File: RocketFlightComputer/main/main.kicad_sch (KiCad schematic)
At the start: 66 parts, among them Y1 32.768kHz, Y5 XRCGB24M000F2P29R0

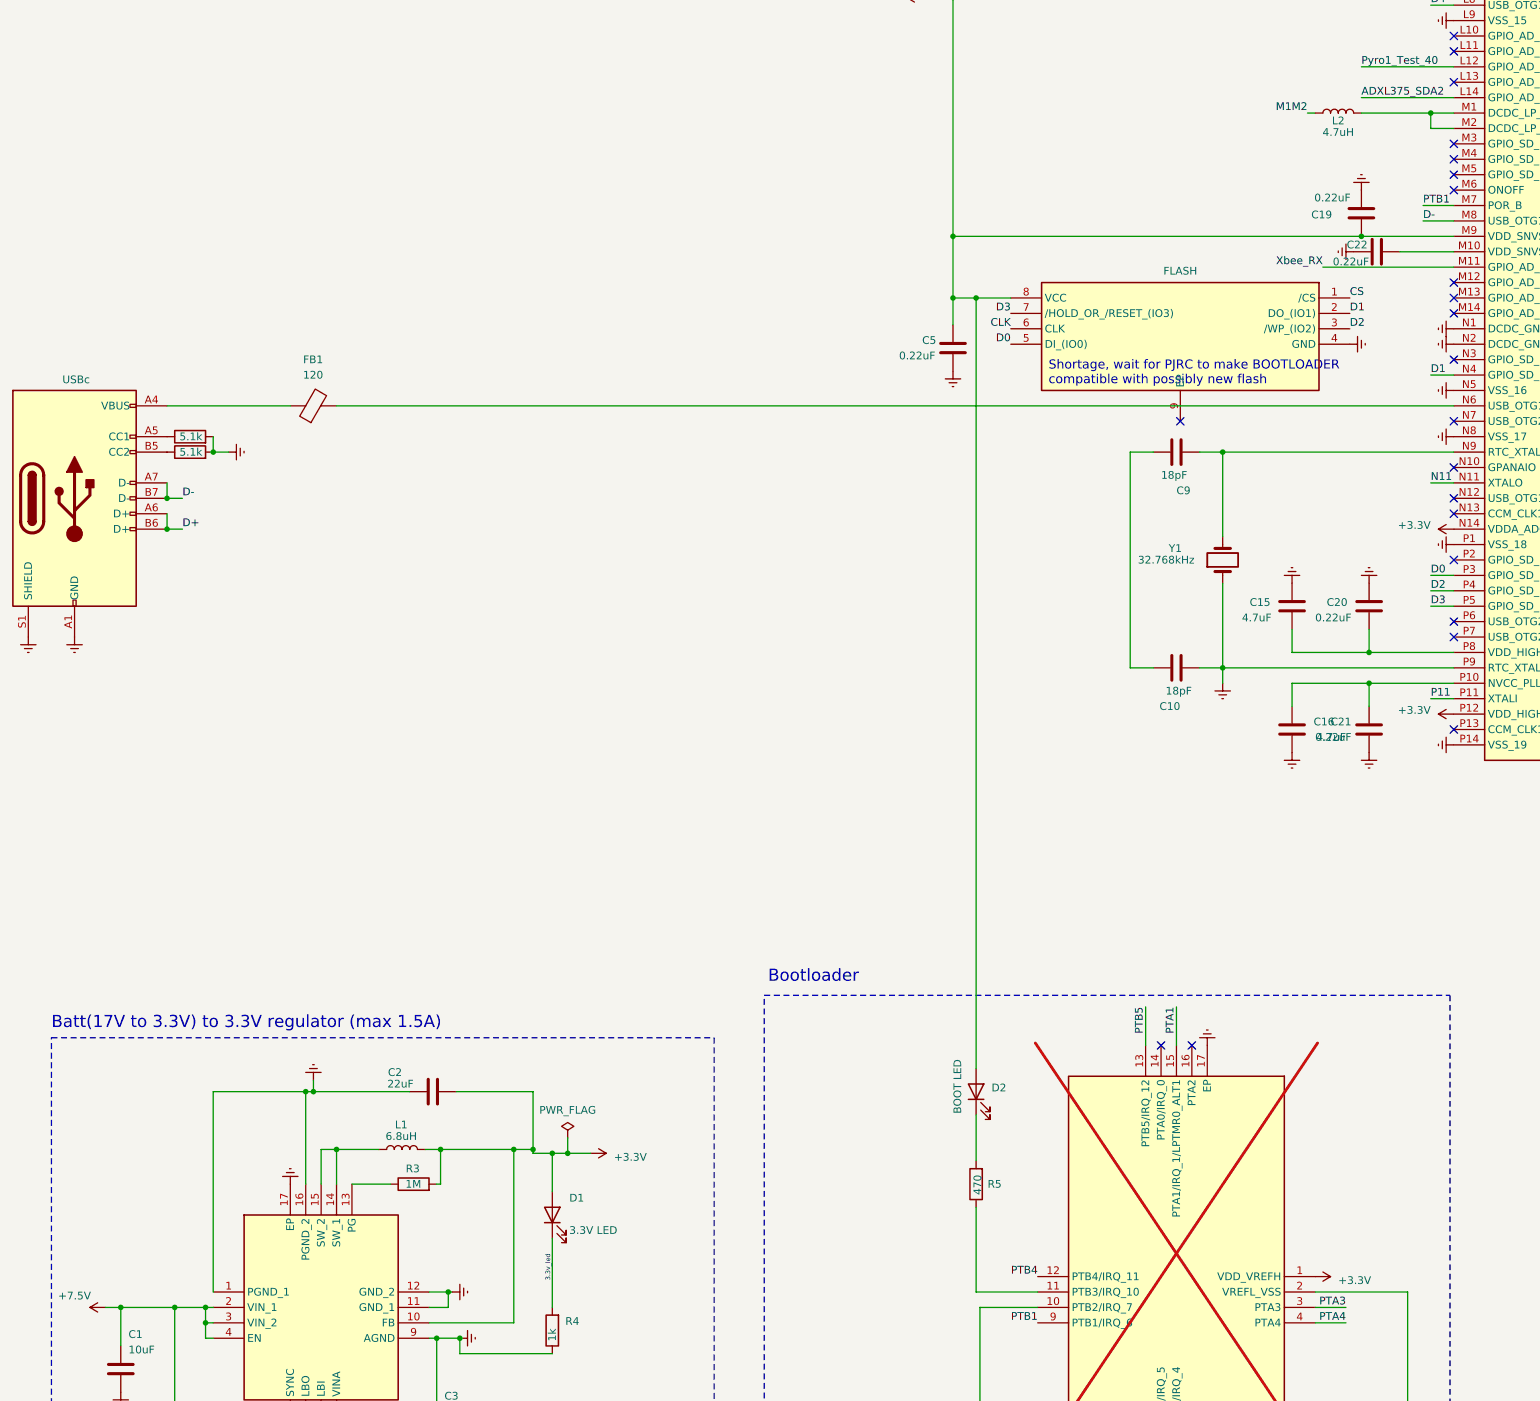
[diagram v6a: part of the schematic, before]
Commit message: Change of winbond flash to other one supported by teensy bootloader since winbond is out of stock
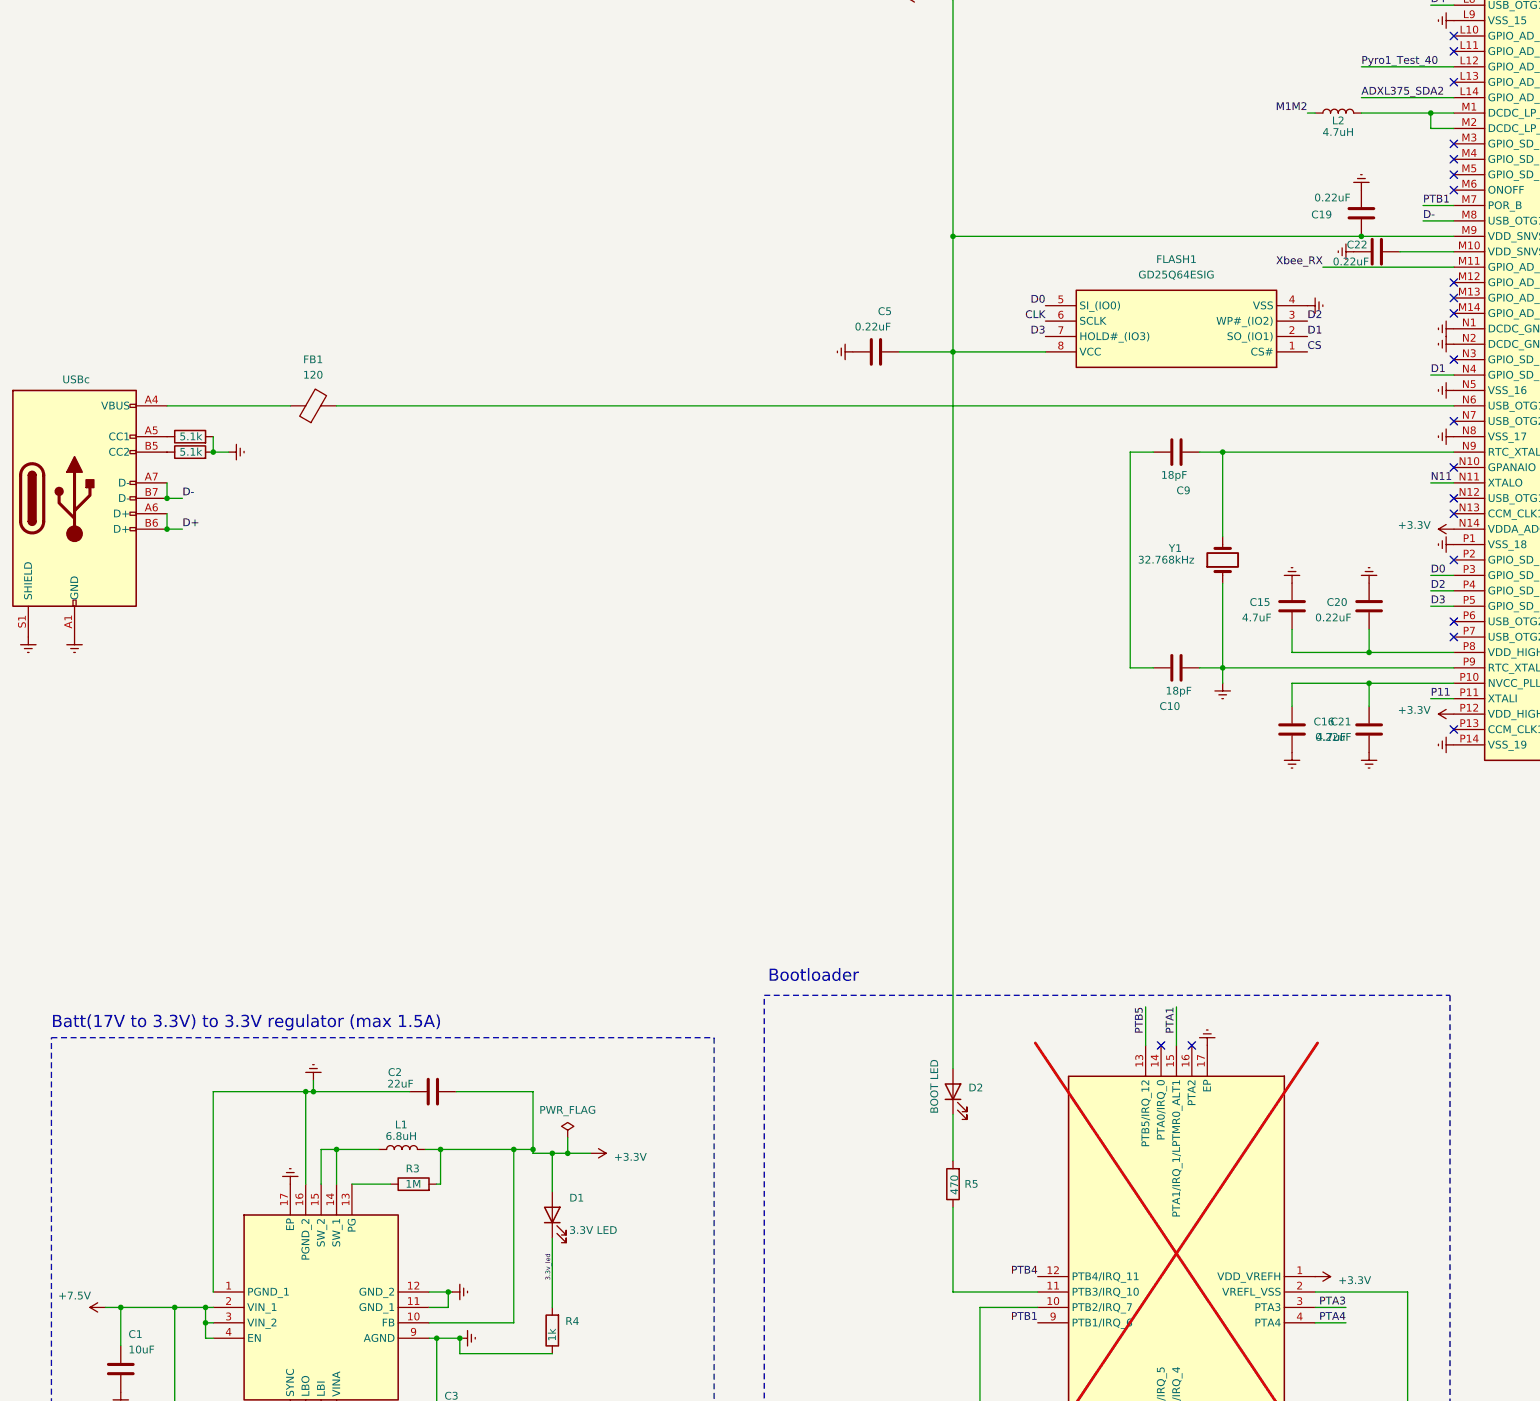
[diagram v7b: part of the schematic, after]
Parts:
- removed W25Q64JVXGIM_TR1: FLASH, footprint:SON80P400X400X50-9N, symbol W25Q64JVXGIM_TR:W25Q64JVXGIM_TR
- added FLASH1: GD25Q64ESIG, footprint:GD25Q64ESIG, symbol GD25Q64ESIG:GD25Q64ESIG
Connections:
- net +3.3V: now also FLASH1.8 (VCC)
- net CLK: now also FLASH1.6 (SCLK)
- net CS: now also FLASH1.1 (CS#)
- net D0: now also FLASH1.5 (SI_(IO0))
- net D1: now also FLASH1.2 (SO_(IO1))
- net D2: now also FLASH1.3 (WP#_(IO2))
- net D3: now also FLASH1.7 (HOLD#_(IO3))
- net GNDREF: now also FLASH1.4 (VSS)
- no-connect marks 93 -> 92
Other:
- note removed: "Shortage, wait for PJRC to make BOOTLOADER compatible with possibly new flash"
- moved on the sheet: C5, D2, R5

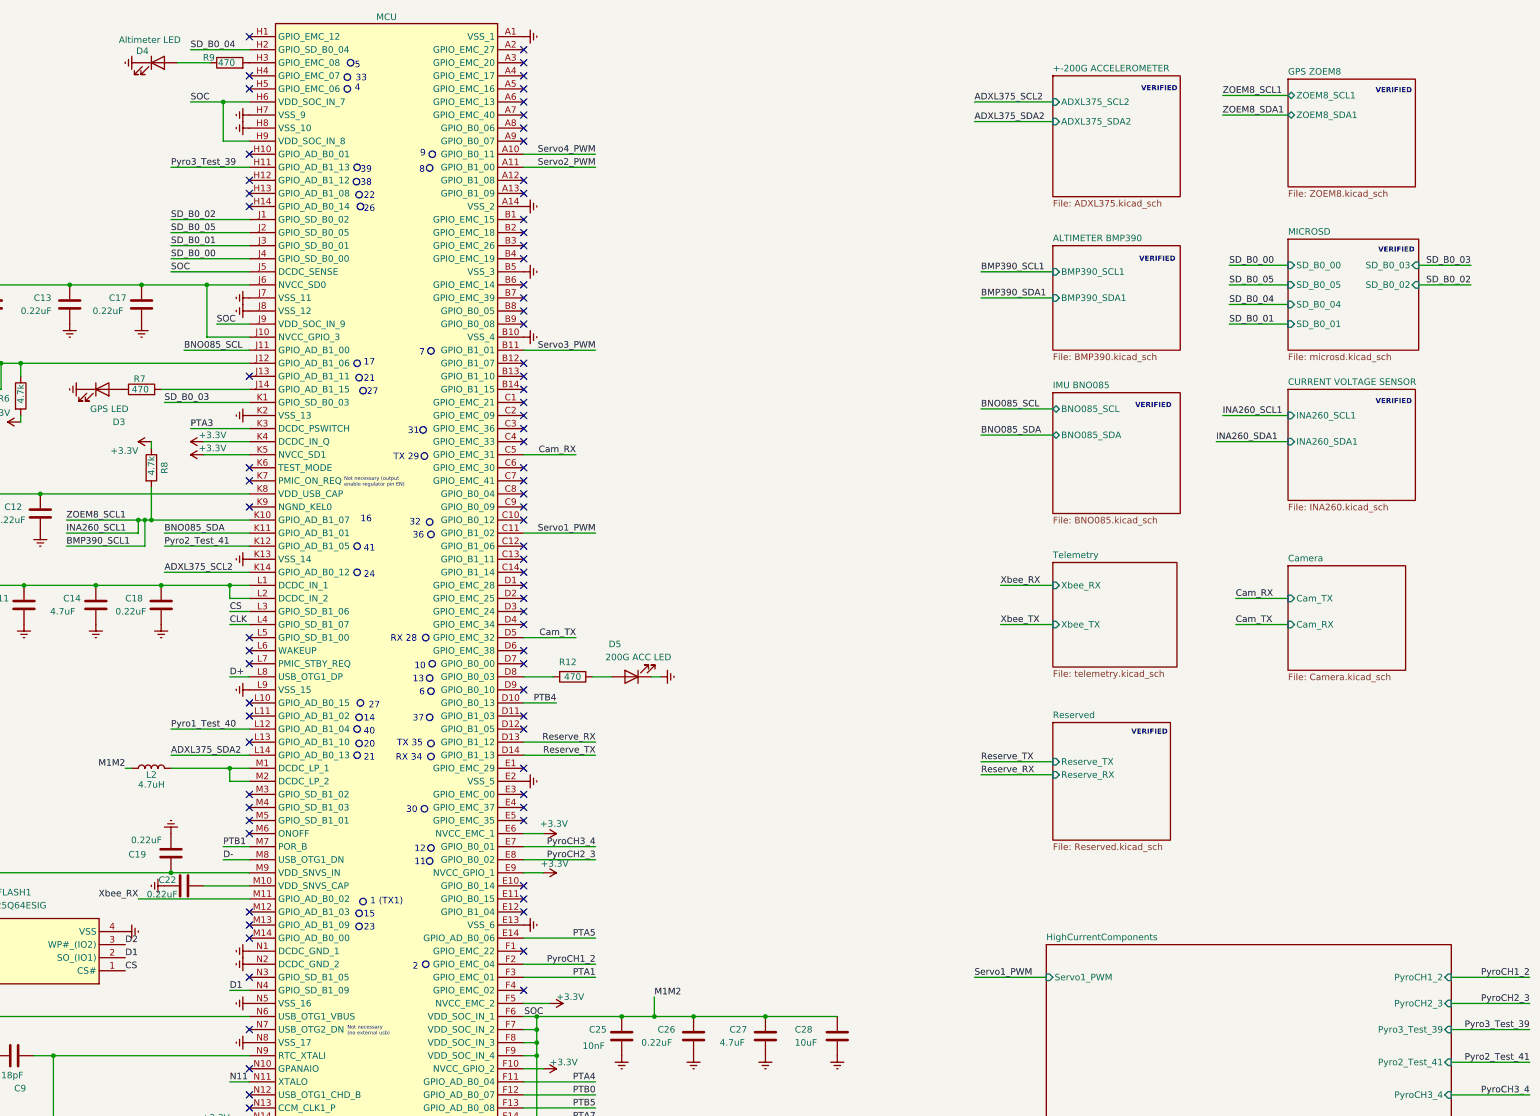
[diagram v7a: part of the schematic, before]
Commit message: Final verification started, schematic verification of USBC and High current components
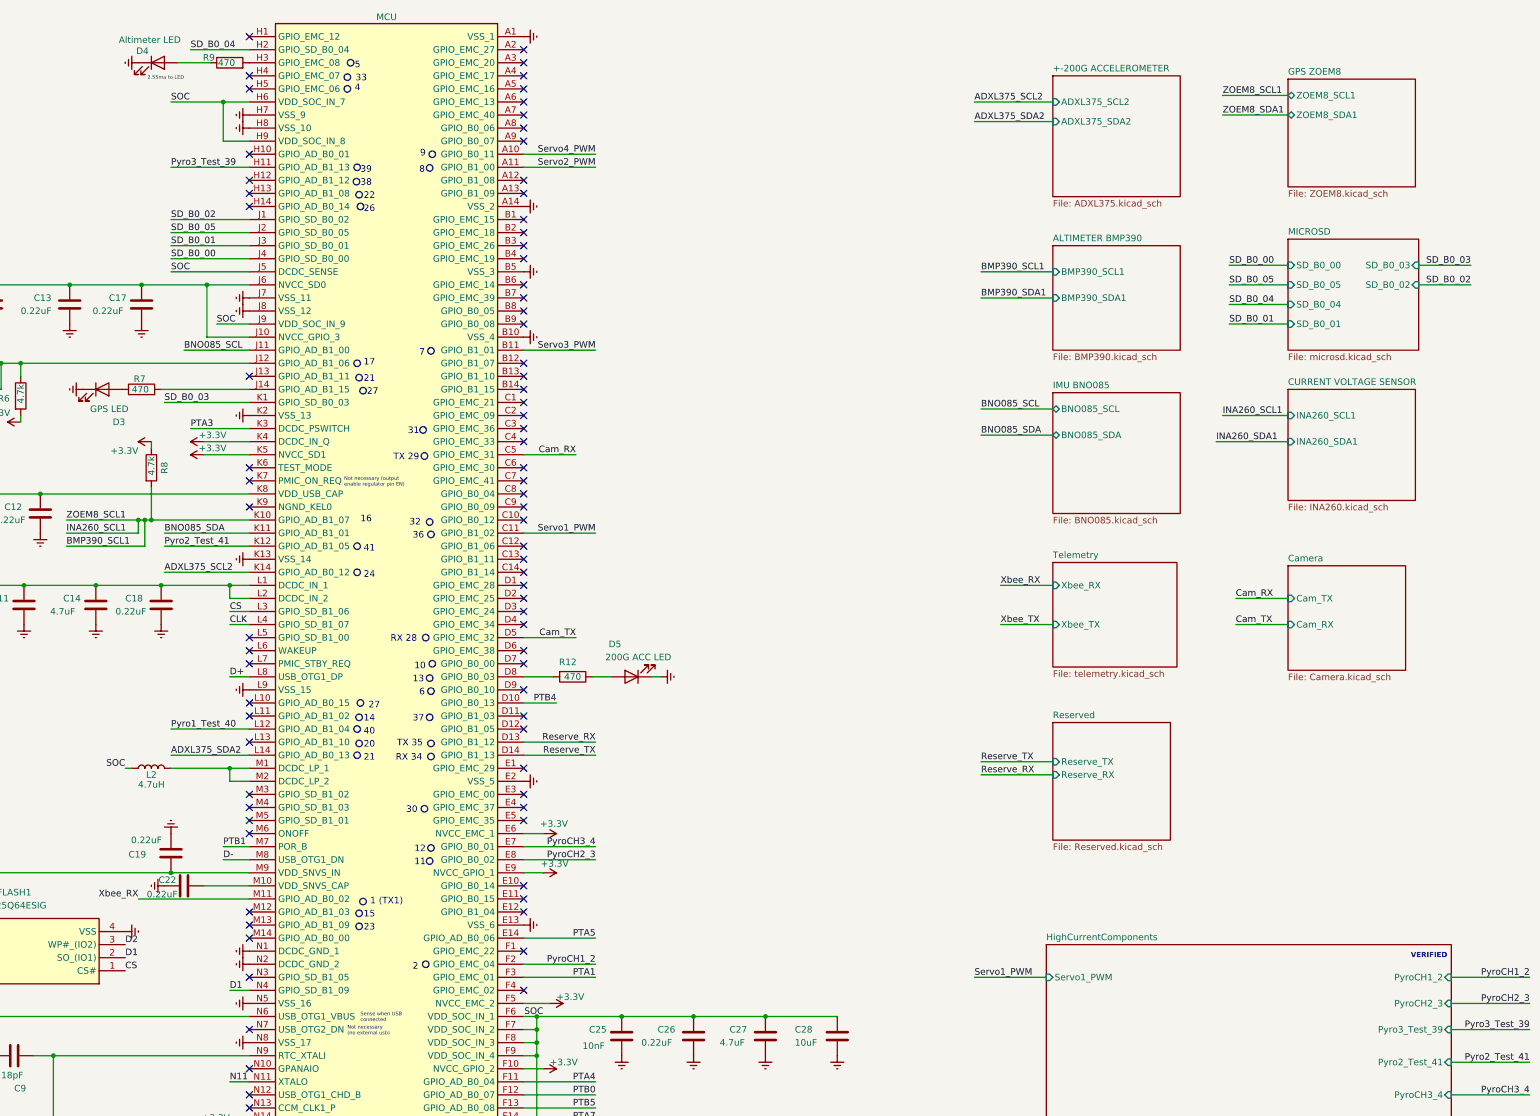
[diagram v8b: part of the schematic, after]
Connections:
- net M1M2 renamed SOC
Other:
- note added: "2.55ma to LED"
- note added: "Sense when USB connected"
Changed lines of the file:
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@@
 		)
 	)
-	(text "Not necessary \n(no external usb)"
+	(text "2.55ma to LED"
 		(exclude_from_sim no)
-		(at 269.24 254 0)
+		(at 230.378 32.258 0)
 		(effects
 			(font
 				(size 0.7 0.7)
 			)
-			(justify left bottom)
+			(justify left)
 		)
 	)
-	(text "VERIFIED"
-		(exclude_from_sim no)
-		(at 469.138 95.758 0)
-		(effects
-			(font
-				(size 1 1)
-				(thickness 0.4)
-				(bold yes)
-			)
-			(justify left bottom)
-		)
-	)
-	(text "VERIFIED"
+	(text "Not necessary \n(no external usb)"
 		(exclude_from_sim no)
-		(at 421.64 160.02 0)
+		(at 269.24 254 0)
 		(effects
 			(font
-				(size 1 1)
-				(thickness 0.4)
-				(bold yes)
+				(size 0.7 0.7)
 			)
 			(justify left bottom)
@@
 		)
 	)
-	(text "VERIFIED"
-		(exclude_from_sim no)
-		(at 423.545 34.925 0)
-		(effects
-			(font
-				(size 1 1)
-				(thickness 0.4)
-				(bold yes)
-			)
-			(justify left bottom)
-		)
-	)
 	(text "31"
 		(exclude_from_sim no)
@@
 		)
 	)
-	(text "VERIFIED"
-		(exclude_from_sim no)
-		(at 469.138 35.306 0)
-		(effects
-			(font
-				(size 1 1)
-				(thickness 0.4)
-				(bold yes)
-			)
-			(justify left bottom)
-		)
-	)
 	(text "37"
 		(exclude_from_sim no)
@@
 		)
 	)
-	(text "VERIFIED"
-		(exclude_from_sim no)
-		(at 469.646 66.294 0)
-		(effects
-			(font
-				(size 1 1)
-				(thickness 0.4)
-				(bold yes)
-			)
-			(justify left bottom)
-		)
-	)
 	(text "TX 29"
 		(exclude_from_sim no)
@@
 		)
 	)
-	(text "VERIFIED"
-		(exclude_from_sim no)
-		(at 423.164 68.072 0)
-		(effects
-			(font
-				(size 1 1)
-				(thickness 0.4)
-				(bold yes)
-			)
-			(justify left bottom)
-		)
-	)
 	(text "6"
 		(exclude_from_sim no)
@@
 		)
 	)
+	(text "Sense when USB \nconnected"
+		(exclude_from_sim no)
+		(at 271.78 214.884 0)
+		(effects
+			(font
+				(size 0.7 0.7)
+			)
+			(justify left)
+		)
+	)
 	(text "21"
 		(exclude_from_sim no)
@@
 		)
 	)
-	(text "VERIFIED"
-		(exclude_from_sim no)
-		(at 422.402 96.52 0)
-		(effects
-			(font
-				(size 1 1)
-				(thickness 0.4)
-				(bold yes)
-			)
-			(justify left bottom)
-		)
-	)
 	(text "15"
 		(exclude_from_sim no)
@@
 		)
 	)
+	(text "VERIFIED"
+		(exclude_from_sim no)
+		(at 475.996 203.454 0)
+		(effects
+			(font
+				(size 1 1)
+				(thickness 0.4)
+				(bold yes)
+			)
+			(justify left bottom)
+		)
+	)
 	(text "Bootloader"
 		(exclude_from_sim no)
@@
 	)
 	(junction
-		(at 328.93 214.63)
-		(diameter 0)
-		(color 0 0 0 0)
-	)
-	(junction
 		(at 212.09 257.81)
 		(diameter 0)
@@
 	)
 	(junction
+		(at 245.11 36.83)
+		(diameter 0)
+		(color 0 0 0 0)
+	)
+	(junction
 		(at 336.55 214.63)
 		(diameter 0)
@@
 	)
 	(junction
-		(at 245.11 36.83)
-		(diameter 0)
-		(color 0 0 0 0)
-	)
-	(junction
 		(at 39.37 363.22)
 		(diameter 0)
@@
 	(wire
 		(pts
-			(xy 328.93 214.63) (xy 336.55 214.63)
+			(xy 322.58 214.63) (xy 336.55 214.63)
 		)
 		(stroke
@@
 	(wire
 		(pts
-			(xy 322.58 214.63) (xy 328.93 214.63)
-		)
-		(stroke
-			(width 0)
-			(type default)
-		)
-	)
-	(wire
-		(pts
 			(xy 66.04 393.7) (xy 66.04 383.54)
 		)
@@
 	(wire
 		(pts
-			(xy 328.93 210.82) (xy 328.93 214.63)
-		)
-		(stroke
-			(width 0)
-			(type default)
-		)
-	)
-	(wire
-		(pts
 			(xy 246.38 135.89) (xy 250.19 135.89)
 		)
@@
 	(wire
 		(pts
-			(xy 238.76 36.83) (xy 245.11 36.83)
+			(xy 234.95 36.83) (xy 245.11 36.83)
 		)
 		(stroke
@@
 		)
 	)
-	(label "M1M2"
+	(label "SOC"
 		(at 226.06 166.37 180)
 		(effects
@@
 		)
 	)
-	(label "M1M2"
-		(at 328.93 210.82 0)
-		(effects
-			(font
-				(size 1.27 1.27)
-			)
-			(justify left bottom)
-		)
-	)
 	(label "SOC"
-		(at 238.76 36.83 0)
+		(at 234.95 36.83 0)
 		(effects
 			(font
